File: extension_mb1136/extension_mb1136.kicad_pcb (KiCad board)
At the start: 2 copper layers, 70 x 57.5 mm, 31 parts, among them CN1 Conn_02x19_Odd_Even, CN2 Conn_02x19_Odd_Even, CN3 Conn_01x08, CN4 Conn_01x06, CN5 Conn_01x08, CN6 Conn_01x10, J1 Conn_01x03, J2 Conn_01x03, Q1 S9013, SW1 USB_SEL, SW2 USB_SEL, U1 STMPS2151MTR, U2 USBLC6-2

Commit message: update pcb
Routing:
- net GND: track 20.6 -> 17.0 mm, vias 214 -> 227
- net PB10: track 41.2 -> 42.7 mm
- net Net-(CNUSB_1-Pad3): track 21.0 -> 22.0 mm
- net Net-(CNUSB_1-Pad2): track 26.9 -> 27.5 mm
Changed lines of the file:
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@@
     (thickness 1.6)
     (drawings 6)
-    (tracks 471)
+    (tracks 481)
     (zones 0)
     (modules 31)
@@
   (gr_arc (start 25.15 101.1) (end 25.15 104.1) (angle 90) (layer Edge.Cuts) (width 0.05))
   (gr_arc (start 89.15 101.1) (end 89.15 104.1) (angle -90) (layer Edge.Cuts) (width 0.05))
+  (via (at 25.4 101.6) (size 0.8) (drill 0.4) (layers F.Cu B.Cu) (net 2))
+  (via (at 88.9 101.6) (size 0.8) (drill 0.4) (layers F.Cu B.Cu) (net 2))
+  (via (at 35.56 91.44) (size 0.8) (drill 0.4) (layers F.Cu B.Cu) (net 2))
+  (via (at 48.26 96.52) (size 0.8) (drill 0.4) (layers F.Cu B.Cu) (net 2))
+  (via (at 50.8 96.52) (size 0.8) (drill 0.4) (layers F.Cu B.Cu) (net 2))
+  (via (at 38.1 96.52) (size 0.8) (drill 0.4) (layers F.Cu B.Cu) (net 2))
+  (via (at 40.64 83.82) (size 0.8) (drill 0.4) (layers F.Cu B.Cu) (net 2))
+  (via (at 43.18 81.28) (size 0.8) (drill 0.4) (layers F.Cu B.Cu) (net 2))
+  (via (at 43.18 83.82) (size 0.8) (drill 0.4) (layers F.Cu B.Cu) (net 2))
+  (via (at 53.34 88.9) (size 0.8) (drill 0.4) (layers F.Cu B.Cu) (net 2))
+  (via (at 60.96 86.36) (size 0.8) (drill 0.4) (layers F.Cu B.Cu) (net 2))
+  (via (at 63.5 86.36) (size 0.8) (drill 0.4) (layers F.Cu B.Cu) (net 2))
+  (via (at 60.96 88.9) (size 0.8) (drill 0.4) (layers F.Cu B.Cu) (net 2))
   (segment (start 45.72 61.56) (end 46.99 61.56) (width 0.5) (layer F.Cu) (net 1))
   (segment (start 46.99 61.56) (end 48.26 61.56) (width 0.5) (layer F.Cu) (net 1))
@@
   (via (at 30.48 60.96) (size 0.8) (drill 0.4) (layers F.Cu B.Cu) (net 2))
   (via (at 30.48 63.5) (size 0.8) (drill 0.4) (layers F.Cu B.Cu) (net 2))
-  (segment (start 38.1 71.12) (end 35.56 68.58) (width 0.5) (layer B.Cu) (net 2))
   (via (at 81.28 101.6) (size 0.8) (drill 0.4) (layers F.Cu B.Cu) (net 2))
   (via (at 83.82 101.6) (size 0.8) (drill 0.4) (layers F.Cu B.Cu) (net 2))
@@
   (segment (start 81.28 86.36) (end 86.36 86.36) (width 0.5) (layer F.Cu) (net 48))
   (segment (start 81.28 83.82) (end 86.36 83.82) (width 0.5) (layer F.Cu) (net 50))
-  (via (at 63.5 83.82) (size 0.8) (drill 0.4) (layers F.Cu B.Cu) (net 50))
+  (via (at 60.96 83.82) (size 0.8) (drill 0.4) (layers F.Cu B.Cu) (net 50))
   (segment (start 65.913 83.82) (end 81.28 83.82) (width 0.5) (layer B.Cu) (net 50))
   (segment (start 57.53 99.1215) (end 57.53 94.362) (width 0.25) (layer F.Cu) (net 50))
   (segment (start 65.913 83.82) (end 63.5 83.82) (width 0.5) (layer B.Cu) (net 50))
-  (segment (start 63.5 83.82) (end 58.42 88.9) (width 0.5) (layer F.Cu) (net 50))
   (segment (start 58.42 88.9) (end 58.42 93.472) (width 0.5) (layer F.Cu) (net 50))
   (segment (start 57.53 94.362) (end 58.42 93.472) (width 0.25) (layer F.Cu) (net 50))
   (segment (start 58.42 93.472) (end 58.989 93.472) (width 0.25) (layer F.Cu) (net 50))
+  (segment (start 60.96 83.82) (end 63.5 83.82) (width 0.5) (layer B.Cu) (net 50))
+  (segment (start 58.42 88.9) (end 58.42 86.36) (width 0.5) (layer F.Cu) (net 50))
+  (segment (start 58.42 86.36) (end 60.96 83.82) (width 0.5) (layer F.Cu) (net 50))
   (segment (start 81.28 81.28) (end 86.36 81.28) (width 0.5) (layer F.Cu) (net 52))
   (segment (start 81.28 74.68) (end 82.935 74.68) (width 0.5) (layer F.Cu) (net 54))
@@
   (segment (start 61.468 57.023) (end 62.992 57.023) (width 0.5) (layer F.Cu) (net 71))
   (segment (start 62.992 57.023) (end 64.135 55.88) (width 0.5) (layer F.Cu) (net 71))
-  (segment (start 45.847 84.074) (end 45.847 82.073) (width 0.5) (layer F.Cu) (net 73))
-  (segment (start 48.387 86.614) (end 45.847 84.074) (width 0.5) (layer F.Cu) (net 73))
-  (segment (start 45.847 82.073) (end 47.46 80.46) (width 0.5) (layer F.Cu) (net 73))
-  (segment (start 53.467 86.614) (end 53.594 86.614) (width 0.5) (layer F.Cu) (net 73))
-  (segment (start 53.467 86.614) (end 48.387 86.614) (width 0.5) (layer F.Cu) (net 73))
   (segment (start 56.3245 98.8075) (end 56.3245 89.3445) (width 0.25) (layer F.Cu) (net 73))
   (segment (start 56.23 99.1215) (end 56.23 98.902) (width 0.25) (layer F.Cu) (net 73))
   (segment (start 56.23 98.902) (end 56.3245 98.8075) (width 0.25) (layer F.Cu) (net 73))
-  (segment (start 53.467 86.614) (end 53.588037 86.614) (width 0.5) (layer F.Cu) (net 73))
-  (segment (start 56.30499 89.330953) (end 56.30499 89.3445) (width 0.5) (layer F.Cu) (net 73))
-  (segment (start 53.588037 86.614) (end 56.30499 89.330953) (width 0.5) (layer F.Cu) (net 73))
-  (segment (start 53.594 82.296) (end 53.594 85.344) (width 0.5) (layer F.Cu) (net 74))
-  (segment (start 53.624 82.296) (end 55.46 80.46) (width 0.5) (layer F.Cu) (net 74))
-  (segment (start 53.594 82.296) (end 53.624 82.296) (width 0.25) (layer F.Cu) (net 74))
-  (segment (start 56.88 99.1215) (end 56.88 89.932) (width 0.25) (layer F.Cu) (net 74))
-  (segment (start 56.88 89.932) (end 56.88 89.424) (width 0.25) (layer F.Cu) (net 74))
-  (segment (start 56.88 89.424) (end 56.88 88.916) (width 0.25) (layer F.Cu) (net 74))
-  (segment (start 53.594 85.344) (end 53.848 85.344) (width 0.5) (layer F.Cu) (net 74))
-  (segment (start 56.88 88.376) (end 56.88 88.916) (width 0.5) (layer F.Cu) (net 74))
-  (segment (start 53.848 85.344) (end 56.88 88.376) (width 0.5) (layer F.Cu) (net 74))
+  (segment (start 45.847 82.073) (end 45.847 84.074) (width 0.5) (layer F.Cu) (net 73))
+  (segment (start 47.46 80.46) (end 45.847 82.073) (width 0.5) (layer F.Cu) (net 73))
+  (segment (start 45.847 84.074) (end 46.863 85.09) (width 0.5) (layer F.Cu) (net 73))
+  (segment (start 46.863 85.09) (end 53.34 85.09) (width 0.5) (layer F.Cu) (net 73))
+  (segment (start 53.34 85.09) (end 55.88 87.63) (width 0.5) (layer F.Cu) (net 73))
+  (segment (start 56.3245 89.3445) (end 56.3245 88.0745) (width 0.25) (layer F.Cu) (net 73))
+  (segment (start 56.3245 88.0745) (end 55.88 87.63) (width 0.25) (layer F.Cu) (net 73))
+  (segment (start 53.34 81.28) (end 53.34 83.82) (width 0.5) (layer F.Cu) (net 74))
+  (segment (start 53.34 83.82) (end 57.15 87.63) (width 0.5) (layer F.Cu) (net 74))
+  (segment (start 55.46 80.46) (end 54.16 80.46) (width 0.5) (layer F.Cu) (net 74))
+  (segment (start 54.16 80.46) (end 53.34 81.28) (width 0.5) (layer F.Cu) (net 74))
+  (segment (start 56.88 87.9) (end 57.15 87.63) (width 0.25) (layer F.Cu) (net 74))
+  (segment (start 56.88 99.1215) (end 56.88 87.9) (width 0.25) (layer F.Cu) (net 74))
   (segment (start 49.53 66.71) (end 49.53 65.786) (width 0.5) (layer F.Cu) (net 75))
   (segment (start 51.308 64.008) (end 56.849 64.008) (width 0.5) (layer F.Cu) (net 75))
@@
     (connect_pads (clearance 0.508))
     (min_thickness 0.254)
-    (fill (arc_segments 32) (thermal_gap 0.508) (thermal_bridge_width 0.508))
+    (fill yes (arc_segments 32) (thermal_gap 0.508) (thermal_bridge_width 0.508))
     (polygon
       (pts
@@
     (connect_pads (clearance 0.508))
     (min_thickness 0.254)
-    (fill (arc_segments 32) (thermal_gap 0.508) (thermal_bridge_width 0.508))
+    (fill yes (arc_segments 32) (thermal_gap 0.508) (thermal_bridge_width 0.508))
     (polygon
       (pts

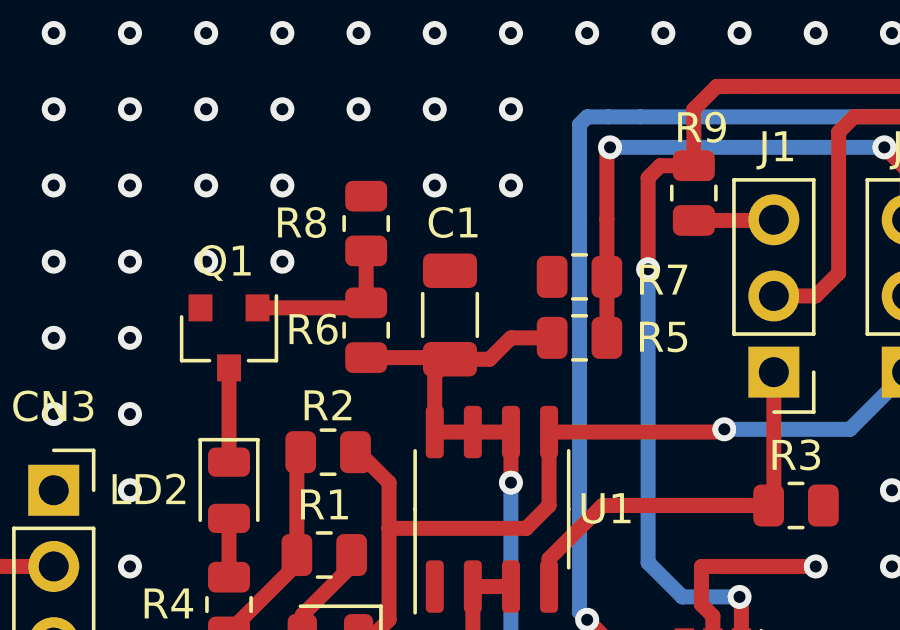
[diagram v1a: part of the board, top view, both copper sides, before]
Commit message: chande footprint for C1. update pcb
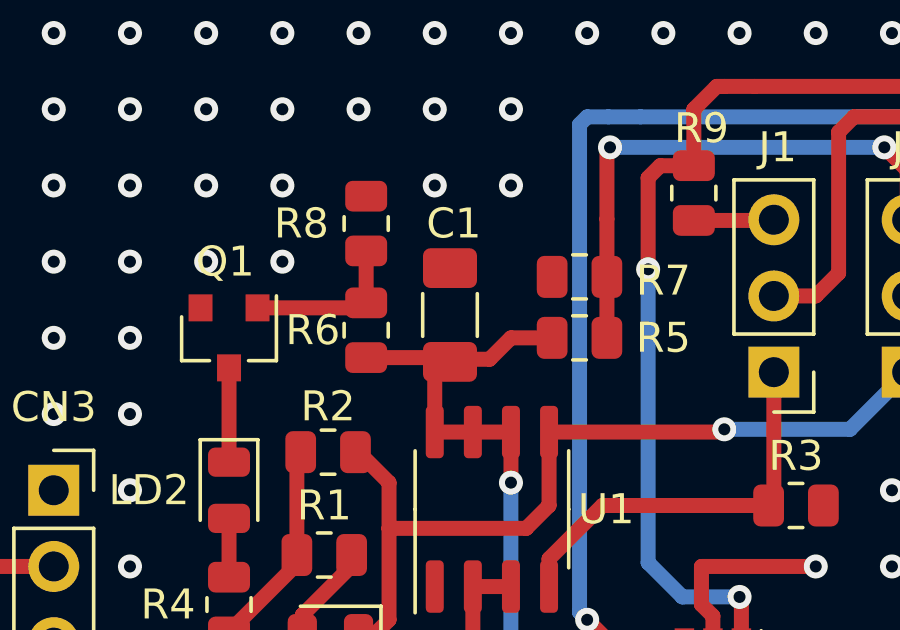
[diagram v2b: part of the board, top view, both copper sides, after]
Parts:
- C1: footprint Capacitor_SMD:C_1206_3216Metric -> Capacitor_SMD:C_1206_3216Metric_Pad1.33x1.80mm_HandSolder
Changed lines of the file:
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@@
     (add_net VIN)
+  )
+  (module Capacitor_SMD:C_1206_3216Metric_Pad1.33x1.80mm_HandSolder (layer F.Cu)
+    (at 46.228 57.658 90)
+    (descr "Capacitor SMD 1206 (3216 Metric), square (rectangular) end terminal, IPC_7351 nominal with elongated pad for handsoldering. (Body size source: IPC-SM-782 page 76, https://www.pcb-3d.com/wordpress/wp-content/uploads/ipc-sm-782a_amendment_1_and_2.pdf), generated with kicad-footprint-generator")
+    (tags "capacitor handsolder")
+    (attr smd)
+    (fp_text reference C1 (at 3.048 0.127 180) (layer F.SilkS)
+      (effects (font (size 1 1) (thickness 0.15)))
+    )
+    (fp_text value 4.7uF (at 0 1.85 90) (layer F.Fab) hide
+      (effects (font (size 1 1) (thickness 0.15)))
+    )
+    (fp_text user %R (at 3.175 0 180) (layer F.Fab)
+      (effects (font (size 0.8 0.8) (thickness 0.12)))
+    )
+    (fp_line (start -1.6 0.8) (end -1.6 -0.8) (layer F.Fab) (width 0.1))
+    (fp_line (start -1.6 -0.8) (end 1.6 -0.8) (layer F.Fab) (width 0.1))
+    (fp_line (start 1.6 -0.8) (end 1.6 0.8) (layer F.Fab) (width 0.1))
+    (fp_line (start 1.6 0.8) (end -1.6 0.8) (layer F.Fab) (width 0.1))
+    (fp_line (start -0.711252 -0.91) (end 0.711252 -0.91) (layer F.SilkS) (width 0.12))
+    (fp_line (start -0.711252 0.91) (end 0.711252 0.91) (layer F.SilkS) (width 0.12))
+    (fp_line (start -2.48 1.15) (end -2.48 -1.15) (layer F.CrtYd) (width 0.05))
+    (fp_line (start -2.48 -1.15) (end 2.48 -1.15) (layer F.CrtYd) (width 0.05))
+    (fp_line (start 2.48 -1.15) (end 2.48 1.15) (layer F.CrtYd) (width 0.05))
+    (fp_line (start 2.48 1.15) (end -2.48 1.15) (layer F.CrtYd) (width 0.05))
+    (pad 2 smd roundrect (at 1.5625 0 90) (size 1.325 1.8) (layers F.Cu F.Paste F.Mask) (roundrect_rratio 0.188679)
+      (net 2 GND))
+    (pad 1 smd roundrect (at -1.5625 0 90) (size 1.325 1.8) (layers F.Cu F.Paste F.Mask) (roundrect_rratio 0.188679)
+      (net 1 PA9))
+    (model ${KISYS3DMOD}/Capacitor_SMD.3dshapes/C_1206_3216Metric.wrl
+      (at (xyz 0 0 0))
+      (scale (xyz 1 1 1))
+      (rotate (xyz 0 0 0))
+    )
   )
   (module Diode_SMD:D_0201_0603Metric (layer F.Cu)
@@
       (net 76 USB_DISCONNECT))
     (model ${KISYS3DMOD}/Connector_PinHeader_2.54mm.3dshapes/PinHeader_1x03_P2.54mm_Vertical.wrl
-      (at (xyz 0 0 0))
-      (scale (xyz 1 1 1))
-      (rotate (xyz 0 0 0))
-    )
-  )
-  (module Capacitor_SMD:C_1206_3216Metric (layer F.Cu)
-    (at 46.228 57.658 90)
-    (descr "Capacitor SMD 1206 (3216 Metric), square (rectangular) end terminal, IPC_7351 nominal, (Body size source: IPC-SM-782 page 76, https://www.pcb-3d.com/wordpress/wp-content/uploads/ipc-sm-782a_amendment_1_and_2.pdf), generated with kicad-footprint-generator")
-    (tags capacitor)
-    (attr smd)
-    (fp_text reference C1 (at 3.048 0.127 180) (layer F.SilkS)
-      (effects (font (size 1 1) (thickness 0.15)))
-    )
-    (fp_text value 4.7uF (at 0 1.85 90) (layer F.Fab) hide
-      (effects (font (size 1 1) (thickness 0.15)))
-    )
-    (fp_line (start 2.3 1.15) (end -2.3 1.15) (layer F.CrtYd) (width 0.05))
-    (fp_line (start 2.3 -1.15) (end 2.3 1.15) (layer F.CrtYd) (width 0.05))
-    (fp_line (start -2.3 -1.15) (end 2.3 -1.15) (layer F.CrtYd) (width 0.05))
-    (fp_line (start -2.3 1.15) (end -2.3 -1.15) (layer F.CrtYd) (width 0.05))
-    (fp_line (start -0.711252 0.91) (end 0.711252 0.91) (layer F.SilkS) (width 0.12))
-    (fp_line (start -0.711252 -0.91) (end 0.711252 -0.91) (layer F.SilkS) (width 0.12))
-    (fp_line (start 1.6 0.8) (end -1.6 0.8) (layer F.Fab) (width 0.1))
-    (fp_line (start 1.6 -0.8) (end 1.6 0.8) (layer F.Fab) (width 0.1))
-    (fp_line (start -1.6 -0.8) (end 1.6 -0.8) (layer F.Fab) (width 0.1))
-    (fp_line (start -1.6 0.8) (end -1.6 -0.8) (layer F.Fab) (width 0.1))
-    (fp_text user %R (at 3.175 0 180) (layer F.Fab)
-      (effects (font (size 0.8 0.8) (thickness 0.12)))
-    )
-    (pad 1 smd roundrect (at -1.475 0 90) (size 1.15 1.8) (layers F.Cu F.Paste F.Mask) (roundrect_rratio 0.2173904347826087)
-      (net 1 PA9))
-    (pad 2 smd roundrect (at 1.475 0 90) (size 1.15 1.8) (layers F.Cu F.Paste F.Mask) (roundrect_rratio 0.2173904347826087)
-      (net 2 GND))
-    (model ${KISYS3DMOD}/Capacitor_SMD.3dshapes/C_1206_3216Metric.wrl
       (at (xyz 0 0 0))
       (scale (xyz 1 1 1))
@@
     (connect_pads (clearance 0.508))
     (min_thickness 0.254)
-    (fill yes (arc_segments 32) (thermal_gap 0.508) (thermal_bridge_width 0.508))
+    (fill (arc_segments 32) (thermal_gap 0.508) (thermal_bridge_width 0.508))
     (polygon
       (pts
@@
     (connect_pads (clearance 0.508))
     (min_thickness 0.254)
-    (fill yes (arc_segments 32) (thermal_gap 0.508) (thermal_bridge_width 0.508))
+    (fill (arc_segments 32) (thermal_gap 0.508) (thermal_bridge_width 0.508))
     (polygon
       (pts
